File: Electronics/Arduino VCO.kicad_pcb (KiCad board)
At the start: 2 copper layers, 29 x 100 mm, 78 parts, among them J9 10-pin power header, SW1 MODE, U1 TL072, U2 AMS1117-5.0

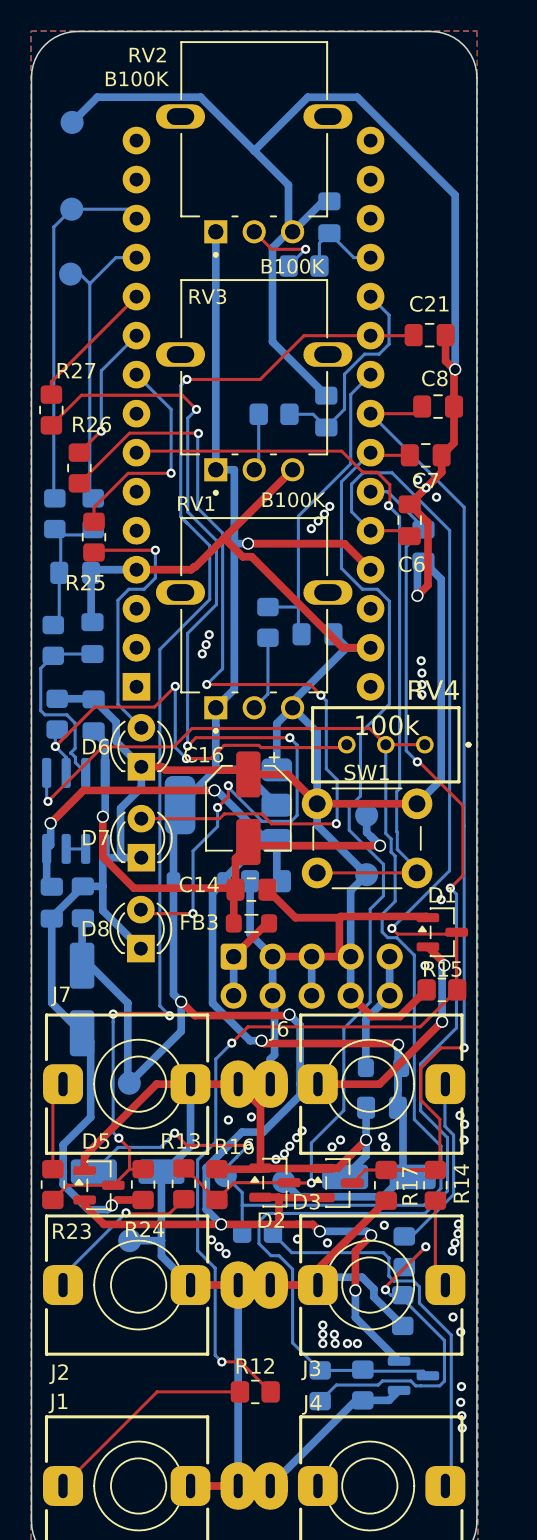
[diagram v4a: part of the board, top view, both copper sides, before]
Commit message: Adding Silkscreen symbols
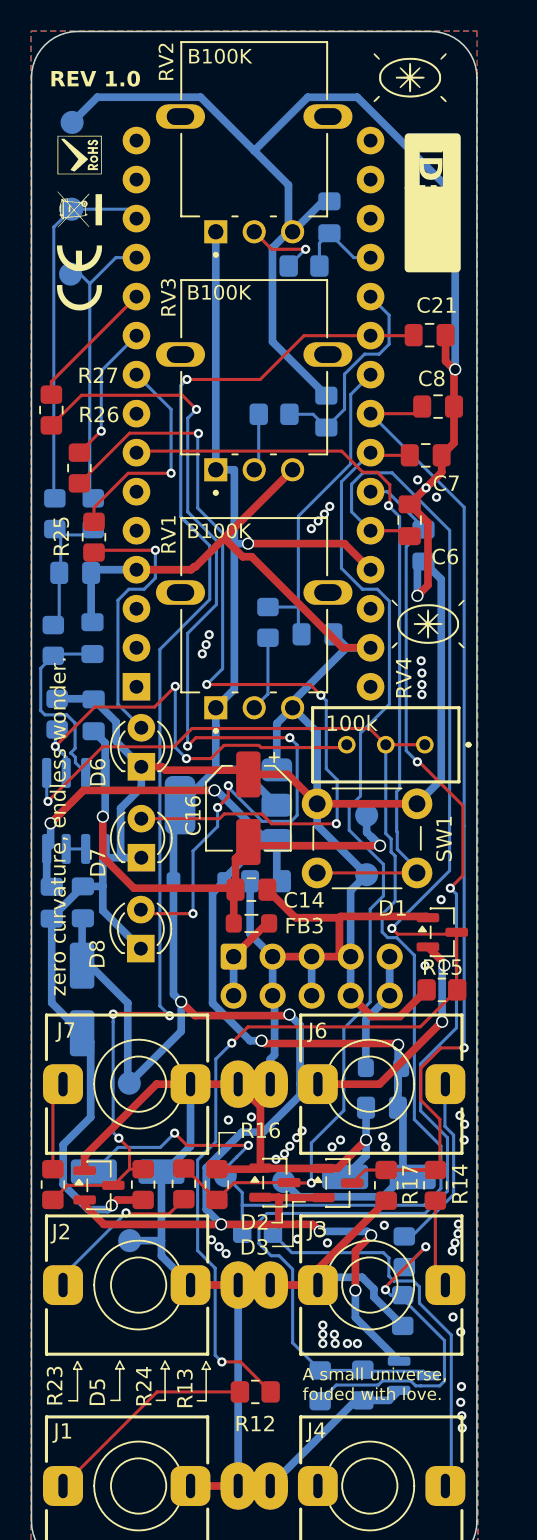
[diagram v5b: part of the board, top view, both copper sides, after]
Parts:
- added G***: LOGO, LOGO, F.Cu at (221.1, 59.0)
- added G***: LOGO, LOGO, F.Cu at (244.3, 85.1)
- added G***: LOGO, LOGO, F.Cu at (243.1, 49.5)
- added G***: LOGO, LOGO, B.Cu at (220.8, 68.9)
- added G***: LOGO, LOGO, B.Cu at (244.2, 89.5)
- added G***: LOGO, LOGO, B.Cu at (227.5, 137.5)
- added G***: LOGO, LOGO, B.Cu at (244.2, 61.8)
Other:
- board text added: "A small universe, folded with love."
- board text added: "CY3-FOLD VCO"
- board text added: "Designed in South Tyrol"
- board text added: "ID:"
- board text added: "In three complex dimensions, even emptiness has a shape."
- board text added: "REV 1.0"
- board text added: "dim_{C}X=3"
- board text added: "zero curvature, endless wonder."
- board text added: "© Nathanael Noir 2026"

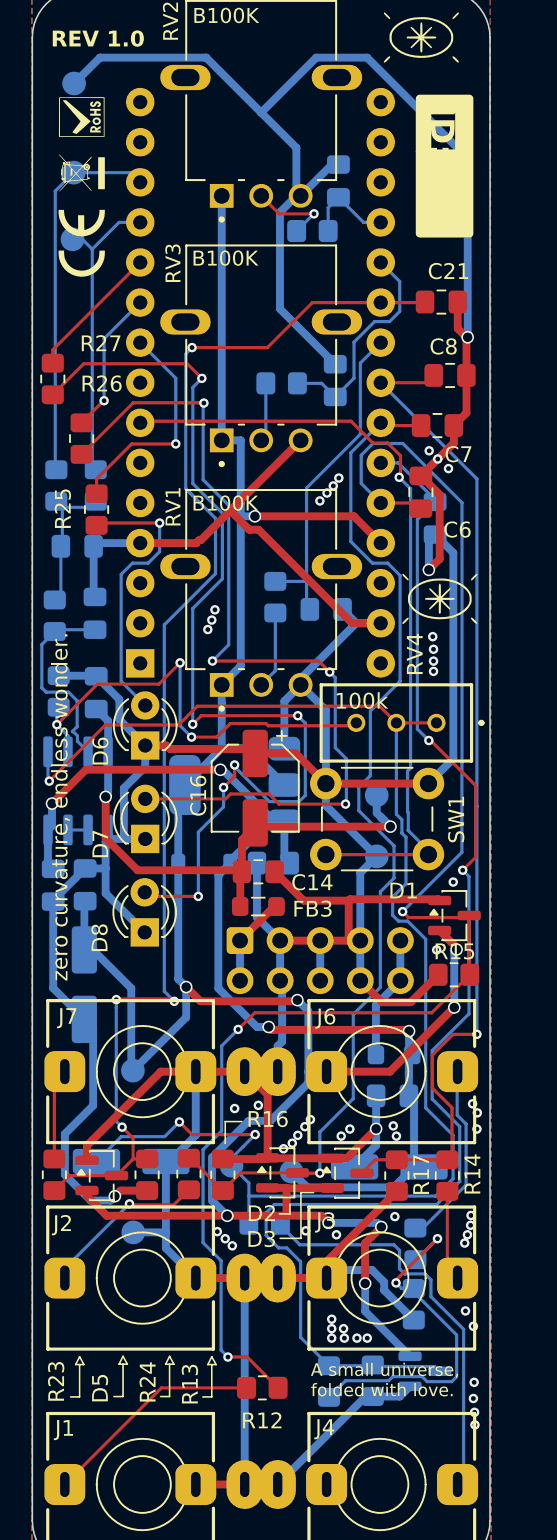
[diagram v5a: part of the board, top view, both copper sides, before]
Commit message: changing silkscreen letter size
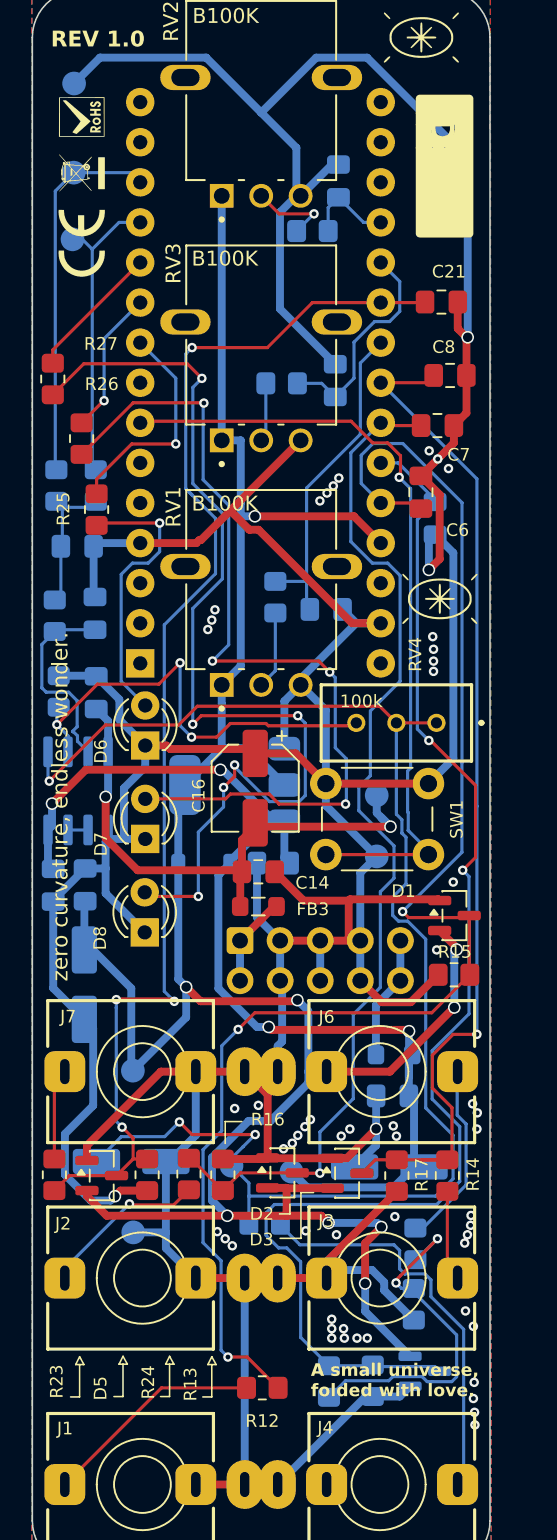
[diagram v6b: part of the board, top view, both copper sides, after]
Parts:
- renumbered TP12 to +12V, TP11 to +5V, TP6 to B, TP7 to C, TP9 to D, TP10 to GND
